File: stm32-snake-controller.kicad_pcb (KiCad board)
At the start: 2 copper layers, 123.5 x 53 mm, 58 parts, among them J101 USB_B_Micro, J102 Conn_01x02, J103 Tag Connector, J104 JST 2.54 Header, J301 Conn_01x03, J302 Conn_01x03, J401 Conn_01x07, J402 Conn_01x07, Q101 AO3501A, SW101 SW_Push, SW102 SW_Push, SW301 SW_SPDT, U101 USBLC6-2SC6, U102 M24C64-RMN, U103 STM32F401RCTx, U201 XC6220B331MR-G, U301 74AHCT1G125, U302 74AHCT1G125, Y101 32.768kHz, Y102 16MHz

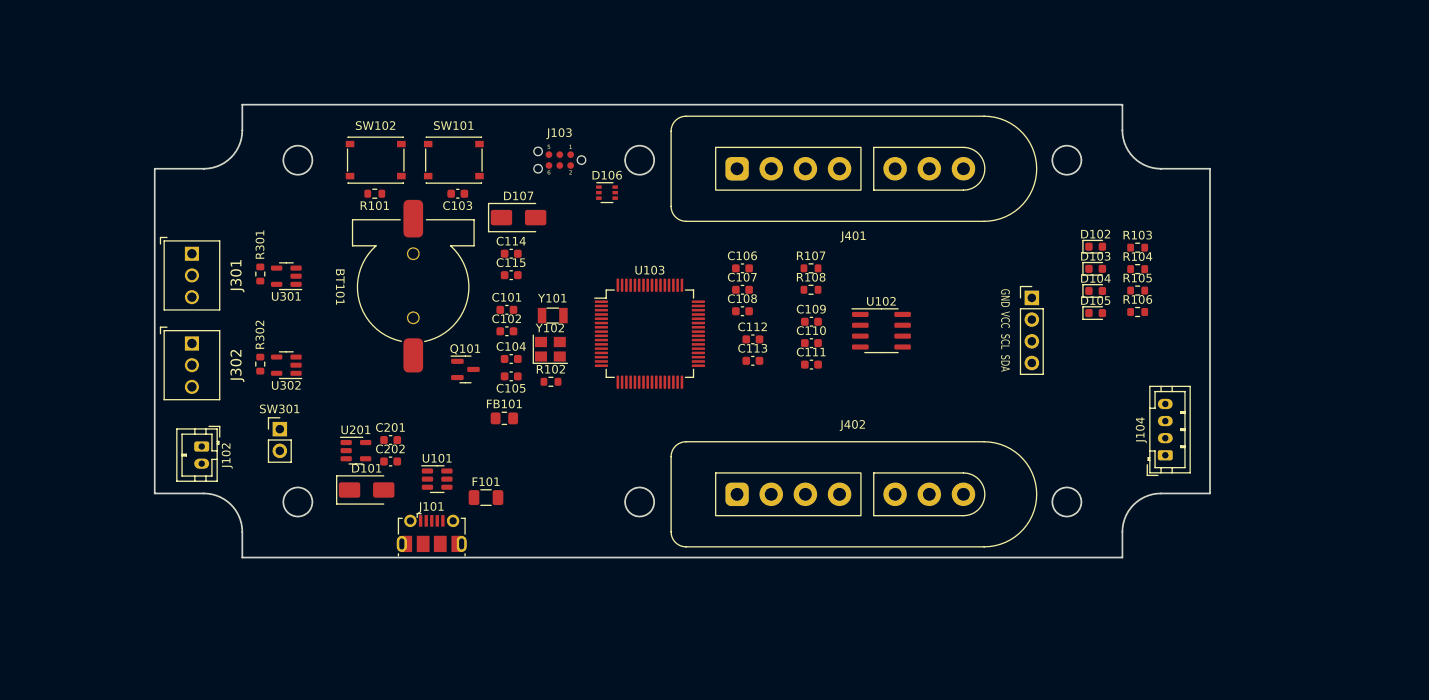
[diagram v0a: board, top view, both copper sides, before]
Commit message: update schematic
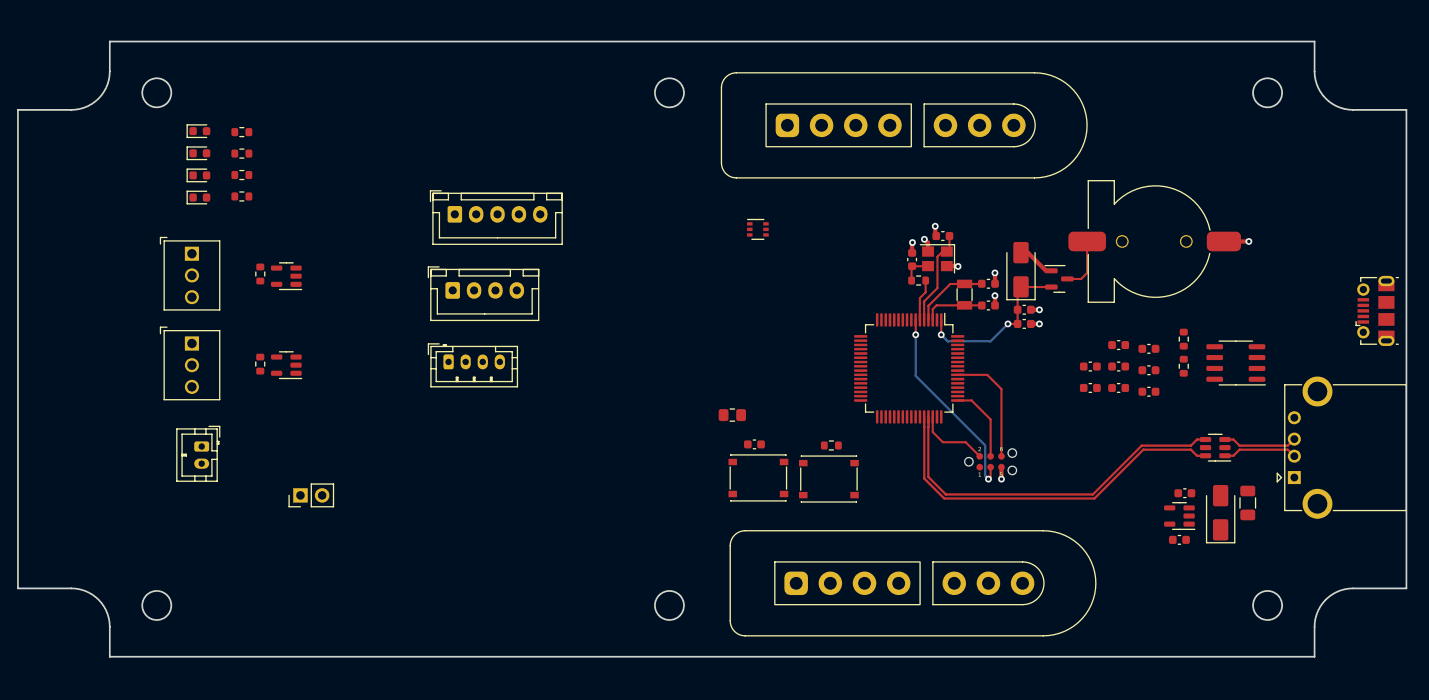
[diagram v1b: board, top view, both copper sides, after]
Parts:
- added J105: USB_A, Connector_USB:USB_A_CONNFLY_DS1095-WNR0, F.Cu at (224.1, 114.9)
- added OLED102: OLED_SPI, Connector_JST:JST_XH_B5B-XH-A_1x05_P2.50mm_Vertical, F.Cu at (125.9, 84.1)
- OLED101: footprint User_Footprint:OLED_128x32_I2C_4pins -> Connector_JST:JST_XH_B4B-XH-A_1x04_P2.50mm_Vertical
- moved J101 113.5 mm to (233.7, 95.4), turned to 90 degrees
- moved D102 105.7 mm to (96.0, 74.3)
- moved D103 105.7 mm to (96.0, 76.9)
- moved D104 105.7 mm to (96.0, 79.5)
- moved D105 105.7 mm to (96.0, 82.1)
- moved R103 105.7 mm to (101.0, 74.5)
- moved R104 105.7 mm to (101.0, 77.0)
- moved R105 105.7 mm to (101.0, 79.5)
- moved R106 105.7 mm to (101.0, 82.0)
- moved D101 100.0 mm to (215.5, 119.0), turned to 90 degrees
- moved U201 96.7 mm to (210.7, 119.4), turned to 180 degrees
- moved C201 93.2 mm to (211.3, 116.7)
- moved C202 92.8 mm to (210.7, 122.2)
- moved U101 91.1 mm to (214.9, 111.4), turned to 180 degrees
- moved F101 89.2 mm to (218.7, 117.9), turned to -90 degrees
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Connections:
- J101 pad 2: /USB_D_N -> unconnected-(J101-D--Pad2)
- J101 pad 3: /USB_D_P -> unconnected-(J101-D+-Pad3)
- U103 pad 21: unconnected-(U103-PA5-Pad21) -> /SPI_CLK
- U103 pad 27: unconnected-(U103-PB1-Pad27) -> /OLED_CE
- U103 pad 57: unconnected-(U103-PB5-Pad57) -> /MOSI
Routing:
- net /D_N: track 0.00 -> 43.8 mm
- net /D_P: track 0.00 -> 43.0 mm
- net /NRST: track 0.00 -> 23.7 mm, vias 0 -> 2
- net /VBAT: track 0.00 -> 19.9 mm, vias 0 -> 2
- net GND: track 0.00 -> 14.1 mm, vias 0 -> 10
- net /SWO: track 0.00 -> 13.7 mm
- net /HSE_IN: track 0.00 -> 11.3 mm
- net /SWCLK: track 0.00 -> 9.09 mm
- net /LSE_OUT: track 0.00 -> 8.97 mm
- net /USB_D_N: track 0.00 -> 8.73 mm
- net /USB_D_P: track 0.00 -> 8.73 mm
- net /SWDIO: track 0.00 -> 8.45 mm
- net /LSE_IN: track 0.00 -> 7.20 mm
- net /BAT+: track 0.00 -> 6.29 mm
- net /HSE_OUT: track 0.00 -> 4.89 mm
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- added copper zone on In1.Cu, net GND
- added copper zone on In2.Cu, net GND
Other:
- board size 123.5 x 53 mm -> 162.5 x 72 mm
- copper layers 2 -> 4

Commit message: replace micro usb to barrel jack
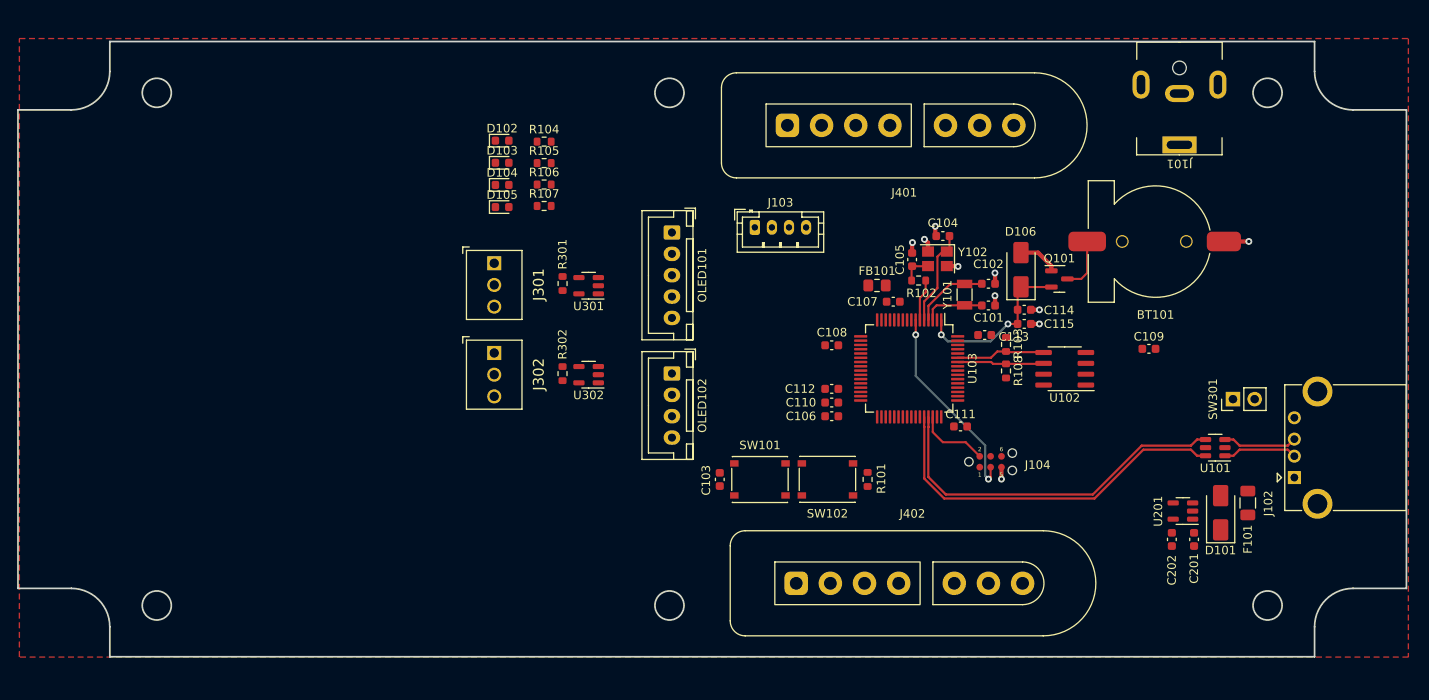
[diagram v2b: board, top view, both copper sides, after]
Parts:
- removed the D106 at (161.4, 85.8)
- removed the J102 at (96.3, 111.3)
- J101: value USB_B_Micro -> Barrel_Jack_MountingPin; footprint Connector_USB:USB_Micro-B_Molex-105017-0001 -> User_Footprint:DC_Power_Jack_PJ-063BH
- moved SW301 109.7 mm to (217.0, 105.7)
- moved J103 39.1 mm to (161.0, 85.6)
- moved C110 37.3 mm to (170.0, 106.1), turned to 180 degrees
- moved D102 35.4 mm to (131.4, 75.5)
- moved D103 35.4 mm to (131.4, 78.0)
- moved D104 35.4 mm to (131.4, 80.6)
- moved D105 35.4 mm to (131.4, 83.2)
- moved R104 35.4 mm to (136.3, 75.6)
- moved R105 35.4 mm to (136.3, 78.1)
- moved R106 35.4 mm to (136.3, 80.6)
- moved R107 35.4 mm to (136.3, 83.1)
- moved R301 35.4 mm to (138.5, 92.2)
- moved U301 35.4 mm to (141.5, 92.4)
- moved U302 35.4 mm to (141.5, 102.8)
- moved J301 35.4 mm to (130.5, 92.3)
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- renumbered D107 to D106, J105 to J102, J104 to J103, J103 to J104, OLED102 to OLED101, OLED101 to OLED102, R107 to R103, R103 to R104, R104 to R105, R105 to R106, R106 to R107
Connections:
- J101 pad 2: unconnected-(J101-D--Pad2) -> GND
- J102 pad 1: VBUS -> +5V
- J103 pad 1: VBUS -> +5V
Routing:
- net /SWO: track 13.7 -> 0.00 mm
- net /SDA: track 0.00 -> 10.4 mm
- net /SCL: track 0.00 -> 10.2 mm
- net /SWCLK: track 9.09 -> 0.00 mm
- added copper zone on F.Cu, net GND
- removed copper zone on In1.Cu, net GND
- removed copper zone on In2.Cu, net GND

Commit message: update SPI pins for OLED
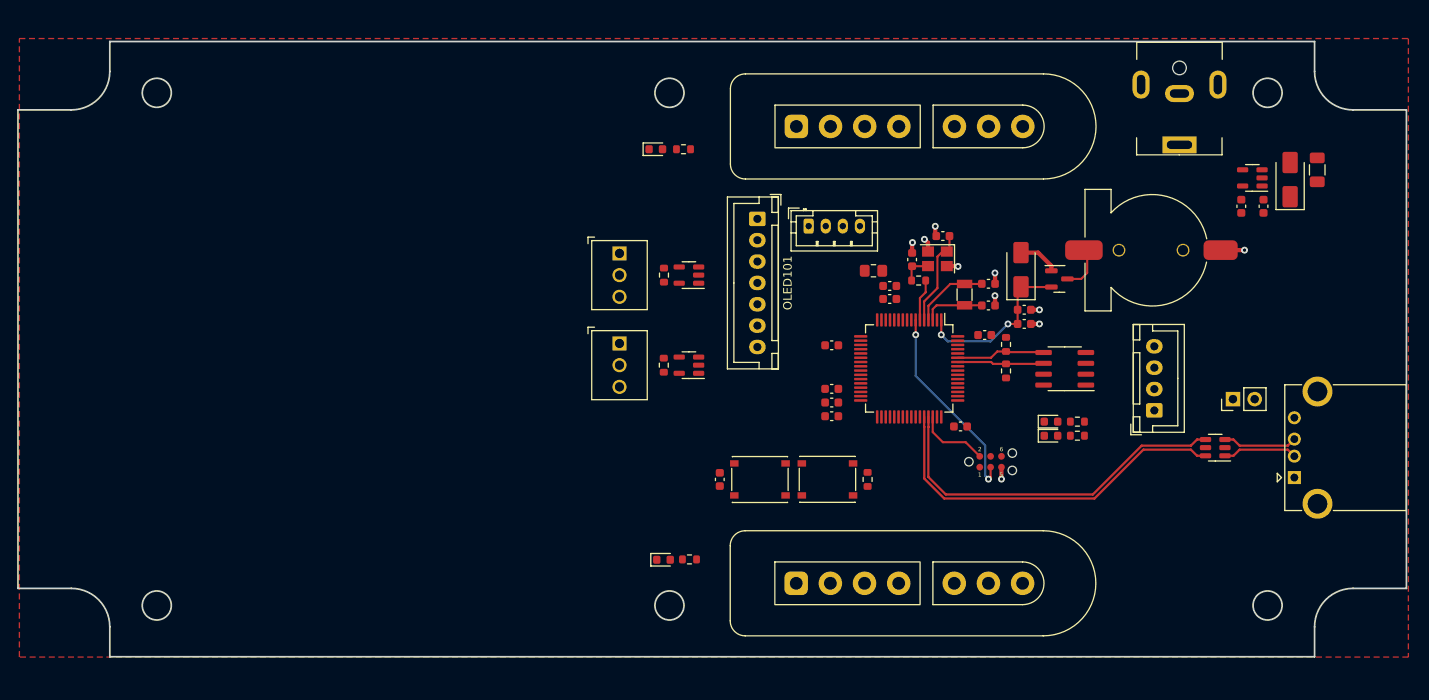
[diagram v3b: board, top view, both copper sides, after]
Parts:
- OLED101: footprint Connector_JST:JST_XH_B5B-XH-A_1x05_P2.50mm_Vertical -> Connector_JST:JST_XH_B7B-XH-A_1x07_P2.50mm_Vertical
- moved D102 72.2 mm to (195.7, 108.3)
- moved R104 70.5 mm to (198.8, 108.3)
- moved D105 69.6 mm to (195.7, 110.0)
- moved R107 68.0 mm to (198.8, 110.0)
- moved OLED102 56.6 mm to (207.8, 107.0), turned to 90 degrees
- moved D103 50.2 mm to (150.3, 124.5)
- moved R105 49.4 mm to (153.4, 124.5)
- moved C201 39.8 mm to (220.5, 83.1)
- moved C202 39.8 mm to (217.9, 83.1)
- moved D101 39.8 mm to (223.6, 80.0)
- moved F101 39.8 mm to (226.8, 78.9)
- moved U201 39.8 mm to (219.2, 79.8)
- moved C109 30.9 mm to (176.8, 94.0)
- moved D104 18.5 mm to (149.4, 76.5)
- moved R106 16.8 mm to (152.7, 76.5)
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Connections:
- OLED101 pad 3: /MOSI -> /SPI_CLK
- OLED101 pad 4: /SPI_CLK -> /MOSI
- OLED101 pad 5: /OLED_CE -> /OLED_RST
- U103 pad 23: /LED_HB -> /OLED_RST
- U103 pad 28: unconnected-(U103-PB2-Pad28) -> /OLED_DC
- U103 pad 53: unconnected-(U103-PC12-Pad53) -> /LED_HB
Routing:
- net /BAT+: track 6.29 -> 5.43 mm

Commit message: add power switch for USB Host
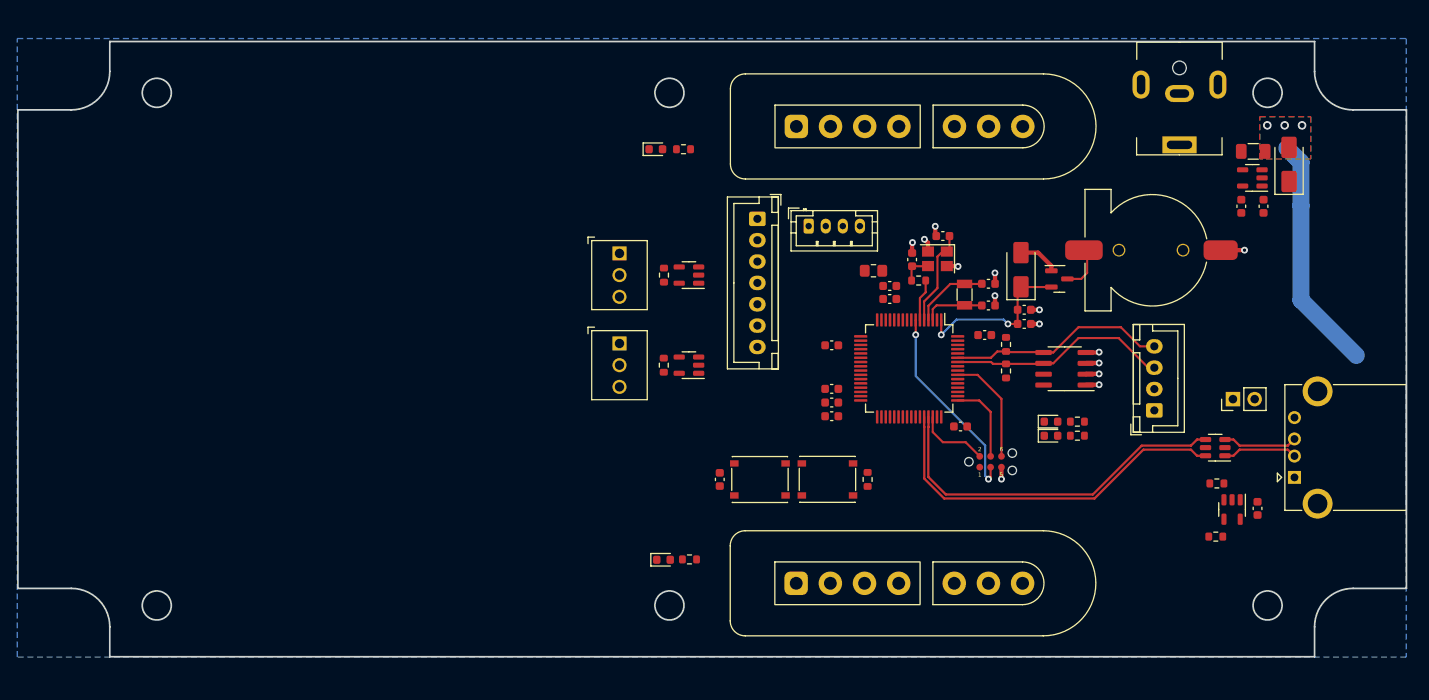
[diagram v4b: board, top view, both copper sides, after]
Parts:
- removed the J102 at (224.1, 114.9)
- added C501: 4.7uF, Capacitor_SMD:C_0603_1608Metric, F.Cu at (219.8, 118.5)
- added J501: USB_A, Connector_USB:USB_A_CONNFLY_DS1095-WNR0, F.Cu at (224.2, 114.9)
- added R501: 10K, Resistor_SMD:R_0603_1608Metric, F.Cu at (214.9, 121.8)
- added R502: 10K, Resistor_SMD:R_0603_1608Metric, F.Cu at (215.1, 115.6)
- added U501: STMPS2141STR, Package_TO_SOT_SMD:SOT-23-5, F.Cu at (216.9, 118.6)
- moved F101 7.80 mm to (219.3, 76.7), turned to 0 degrees
- moved D101 1.78 mm to (223.5, 78.2)
- renumbered J103 to J102, J104 to J103
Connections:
- U103 pad 41: unconnected-(U103-PA8-Pad41) -> /USB_OTG_EN
- U103 pad 42: unconnected-(U103-PA9-Pad42) -> /USB_OTG_VSEN
- U103 pad 43: unconnected-(U103-PA10-Pad43) -> /USB_OTG_OC
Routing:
- net (no net): track 0.00 -> 27.6 mm
- net /SCL: track 10.2 -> 25.8 mm
- net /SDA: track 10.4 -> 25.5 mm
- net /SWO: track 0.00 -> 13.0 mm
- net /SWCLK: track 0.00 -> 9.61 mm
- net GND: track 14.0 -> 20.2 mm, vias 10 -> 14
- net +5V: vias 0 -> 3
- added copper zone on B.Cu, net +3V3
- added copper zone on B.Cu, net +5V
- added copper zone on F.Cu, net +5V
- added copper zone on In1.Cu, net GND
- added copper zone on In2.Cu, net GND
- removed copper zone on F.Cu, net GND

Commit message: update PCB design
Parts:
- removed the R101 at (174.2, 115.1)
- removed SW102: SW_Push, User_Footprint:XKB-Connectivity-TS-1187A-B-A-B
- removed SW301: SW_SPDT, Connector_PinHeader_2.54mm:PinHeader_1x02_P2.54mm_Vertical
- added G***: LOGO, User_Footprint:butler-electronics-15, F.Cu at (147.1, 118.1)
- added H101: MountingHole, MountingHole:MountingHole_3.2mm_M3, F.Cu at (143.0, 68.0)
- added H102: MountingHole, MountingHole:MountingHole_3.2mm_M3, F.Cu at (233.0, 68.0)
- added H103: MountingHole, MountingHole:MountingHole_3.2mm_M3, F.Cu at (233.0, 132.0)
- added H104: MountingHole, MountingHole:MountingHole_3.2mm_M3, F.Cu at (143.0, 132.0)
- added R102: 10K, Resistor_SMD:R_0603_1608Metric, F.Cu at (192.5, 98.5)
- added REF**: KiCad-Logo2_8mm_SilkScreen, Symbol:KiCad-Logo2_8mm_SilkScreen, F.Cu at (163.7, 112.8)
- added REF**: OSHW-Logo_7.5x8mm_SilkScreen, Symbol:OSHW-Logo_7.5x8mm_SilkScreen, F.Cu at (219.5, 98.0)
- added kibuzzard-65A37CF1: G***, kibuzzard-65A37CF1, F.Cu at (196.8, 74.0)
- added kibuzzard-65A37D11: G***, kibuzzard-65A37D11, F.Cu at (196.8, 125.9)
- added kibuzzard-65A37DD1: G***, kibuzzard-65A37DD1, F.Cu at (229.4, 122.0)
- added kibuzzard-65A37F11: G***, kibuzzard-65A37F11, F.Cu at (144.5, 85.1)
- added kibuzzard-65A37F1A: G***, kibuzzard-65A37F1A, F.Cu at (144.5, 107.8)
- J401, J402: footprint User_Footprint:SNES_Controller_Port -> User_Footprint:SNES_Controller_Port_Horizontal
- OLED101: renamed from OLED102; footprint Connector_JST:JST_XH_B4B-XH-A_1x04_P2.50mm_Vertical -> Connector_JST:JST_PH_B4B-PH-K_1x04_P2.00mm_Vertical
- OLED102: renamed from OLED101; footprint Connector_JST:JST_XH_B7B-XH-A_1x07_P2.50mm_Vertical -> Connector_JST:JST_PH_B7B-PH-K_1x07_P2.00mm_Vertical
- moved R103 75.0 mm to (200.9, 66.4)
- moved D104 75.0 mm to (197.7, 66.4), turned to 180 degrees
- moved D105 74.6 mm to (197.7, 133.3), turned to 180 degrees
- moved R104 74.6 mm to (200.9, 133.3)
- moved C110 62.3 mm to (217.4, 129.9), turned to 90 degrees
- moved SW101 53.2 mm to (212.7, 129.9), turned to 180 degrees
- moved J402 49.6 mm to (175.3, 77.8), turned to 180 degrees
- moved J401 48.2 mm to (175.5, 121.8)
- moved R107 23.6 mm to (214.0, 98.7)
- moved R108 23.6 mm to (214.0, 102.4)
- moved OLED102 8.56 mm to (161.4, 93.2)
- moved R501 7.30 mm to (207.8, 115.7), turned to 90 degrees
- moved R502 7.10 mm to (207.9, 120.9), turned to -90 degrees
- moved J102 6.71 mm to (174.0, 84.9), turned to 180 degrees
- moved U301 4.97 mm to (153.7, 96.1)
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- renumbered C114 to C101, C115 to C102, C106 to C103, C108 to C104, C110 to C105, C111 to C106, C113 to C107, C107 to C108, C103 to C110, C101 to C111, C104 to C112, C105 to C113, C102 to C114, C112 to C115, D106 to D102, D102 to D103, D103 to D104, D104 to D105, D105 to D106, R104 to R101, R105 to R103, R106 to R104, R107 to R105, R102 to R106, R103 to R107, R502 to R501, R501 to R502
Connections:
- D104 pad 2: /LED_SNES0 -> /LED_SNES1
- D105 pad 2: /LED_SNES1 -> /LED_SNES0
- J301 pad 3: /LED_PWR -> VBUS
- J302 pad 3: /LED_PWR -> VBUS
- OLED102 pad 2: +3V3 -> +5V
- OLED102 pad 3: /SPI_CLK -> /MOSI
- OLED102 pad 4: /MOSI -> /SPI_CLK
- OLED102 pad 6: /OLED_DC -> /OLED_CE
- OLED102 pad 7: /OLED_CE -> /OLED_DC
- U101 pad 5: VBUS -> /USB_OTG_VSEN
- U103 pad 10: unconnected-(U103-PC2-Pad10) -> /LED_SNES1
- U103 pad 11: unconnected-(U103-PC3-Pad11) -> /SNES_DATA1
- U103 pad 24: /LED_SNES0 -> unconnected-(U103-PC4-Pad24)
- U103 pad 25: /LED_SNES1 -> unconnected-(U103-PC5-Pad25)
- U103 pad 33: /~{EEPROM} -> unconnected-(U103-PB12-Pad33)
- U103 pad 37: /SNES_DATA1 -> unconnected-(U103-PC6-Pad37)
- U103 pad 39: unconnected-(U103-PC8-Pad39) -> /LED_SNES0
- U103 pad 56: unconnected-(U103-PB4-Pad56) -> /~{EEPROM}
- U103 pad 60: /BOOT0 -> Net-(U103-BOOT0)
- U301 pad 2: /LED_GRID0 -> /LED_GRID1
- U302 pad 2: /LED_GRID1 -> /LED_GRID0
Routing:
- net +5V: track 0.00 -> 205.0 mm, vias 3 -> 7
- net VBUS: track 0.00 -> 111.1 mm, vias 0 -> 7
- net /USB_OTG_VSEN: track 0.00 -> 66.5 mm
- net /SNES_CLK: track 0.00 -> 59.4 mm, vias 0 -> 3
- net /SNES_LATCH: track 0.00 -> 53.1 mm, vias 0 -> 1
- net /USB_OTG_EN: track 0.00 -> 48.5 mm
- net GND: track 20.2 -> 67.1 mm, vias 14 -> 60
- net /USB_OTG_OC: track 0.00 -> 46.8 mm
- net /LED_SNES1: track 0.00 -> 44.2 mm
- net /NRST: track 23.7 -> 67.9 mm, vias 2 -> 4
- net /LED_GRID0: track 0.00 -> 41.8 mm, vias 0 -> 2
- net /LED_SNES0: track 0.00 -> 41.5 mm
- net /LED_GRID1: track 0.00 -> 40.7 mm, vias 0 -> 2
- net +3V3: track 4.77 -> 34.5 mm, vias 0 -> 18
- net /SPI_CLK: track 0.00 -> 29.2 mm
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- added copper zone on F.Cu, net +3V3
- added copper zone on F.Cu, net /LDO_3V3/5V
- added copper zone on B.Cu, net VBUS
- added copper zone on F.Cu, net VBUS
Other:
- board size 162.5 x 72 mm -> 98 x 72 mm
- board text added: "${TITLE} by ${COMMENT1} ${ISSUE_DATE}/REV.${REVISION}"
- board text added: "3V3"
- board text added: "5V D G"
- board text added: "5V/5A Max"
- board text added: "CR1220"
- board text added: "G RX TX 5V"
- board text added: "GND"
- board text added: "HB"
- board text added: "I^{2}C"
- board text added: "JLCJLCJLCJLC"
- board text added: "OLED Display"
- board text added: "PWR"
- board text added: "Reset"
- board text added: "SCL"
- board text added: "SDA"
- board text added: "UART"
